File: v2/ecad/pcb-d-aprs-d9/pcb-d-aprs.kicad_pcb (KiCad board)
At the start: 4 copper layers, 100 x 80 mm, 211 parts, among them K1 Omron G6K-2F-Y 5 VDC DPDT sig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, Q1 2N7002 PA_EN -> H/L low (neve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, Q2 2N7002 relay coil, Q3 2N7002, Q4 2N7002, Q5 2N7002, Q6 2N7002, Q7 2N7002, Q8 2N7002, Q9 2N7002, U1 TLV75533PDBV 3.3 V 500 mA LDO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, U10 74LVC1G08 AND: headsets AND s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, U11 74LVC1G04 inverter (2 A 4 Y):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, U12 74LVC1G08 AND: KEY = PTT_ANY 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, U13 74LVC1G04 inverter: KEY -> SA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, U14 74LVC1G08 AND: PA_KEY = KEY A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, U15 TPS22810DRV, U16 PCA9555PW 0x26: COS, PTT stat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, U2 NiceRF SA868 VHF 2 W exciter,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, U3 CP2102N-A02-GQFN28 USB-UART b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, U4 TUSB2046BI four-port USB 2.0 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, U5 USBLC6-2SC6, U6 TI PCM2912A USB audio codec (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, U7 TI TPA6132A2 headphone amplif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, U8 TLV9062IDGK dual op amp (1 OU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, U9 74LVC1G08 AND (1 A 2 B 3 GND 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, Y1 6 MHz 3225 (CL 20 pF; C1 = C2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, Y2 6 MHz 3225 (codec clock; 18 p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

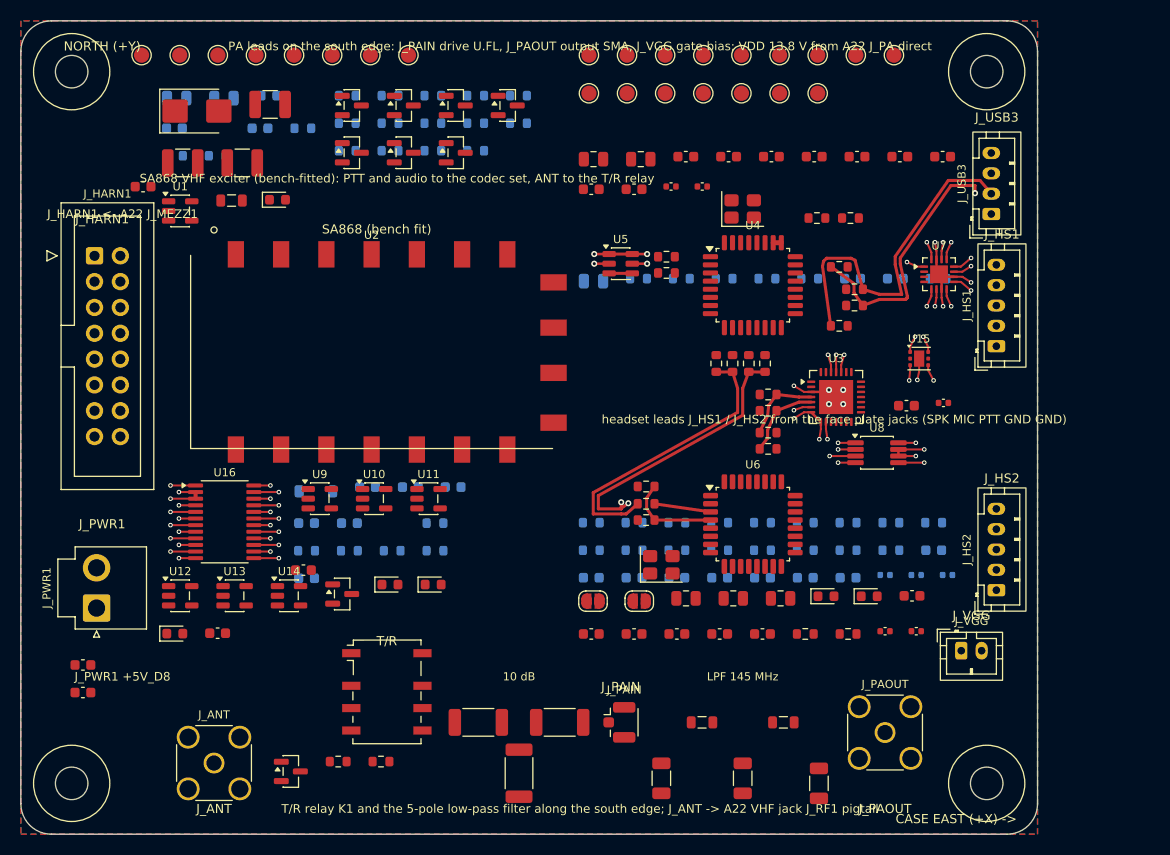
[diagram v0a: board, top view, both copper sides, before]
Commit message: feat(d): D's routed board and its regenerated schematic, tracked [MESHSAT-862]
The board is the best of the D run: 0 hard of the fifteen types, 3 unrouted
before the finish (the finish closes two of them), 5 of 5 pairs laid and
every one within 1 mm, and the schematic carries the harness pin map that
moved USB_D8 to the header's end row.

It is committed as an artefact, not as a deliverable: a routed board that
exists only in a rented box's copy directory exists nowhere, which is how
four of them were lost on 10 September. The one open and what it is are in
appendix 32.128.
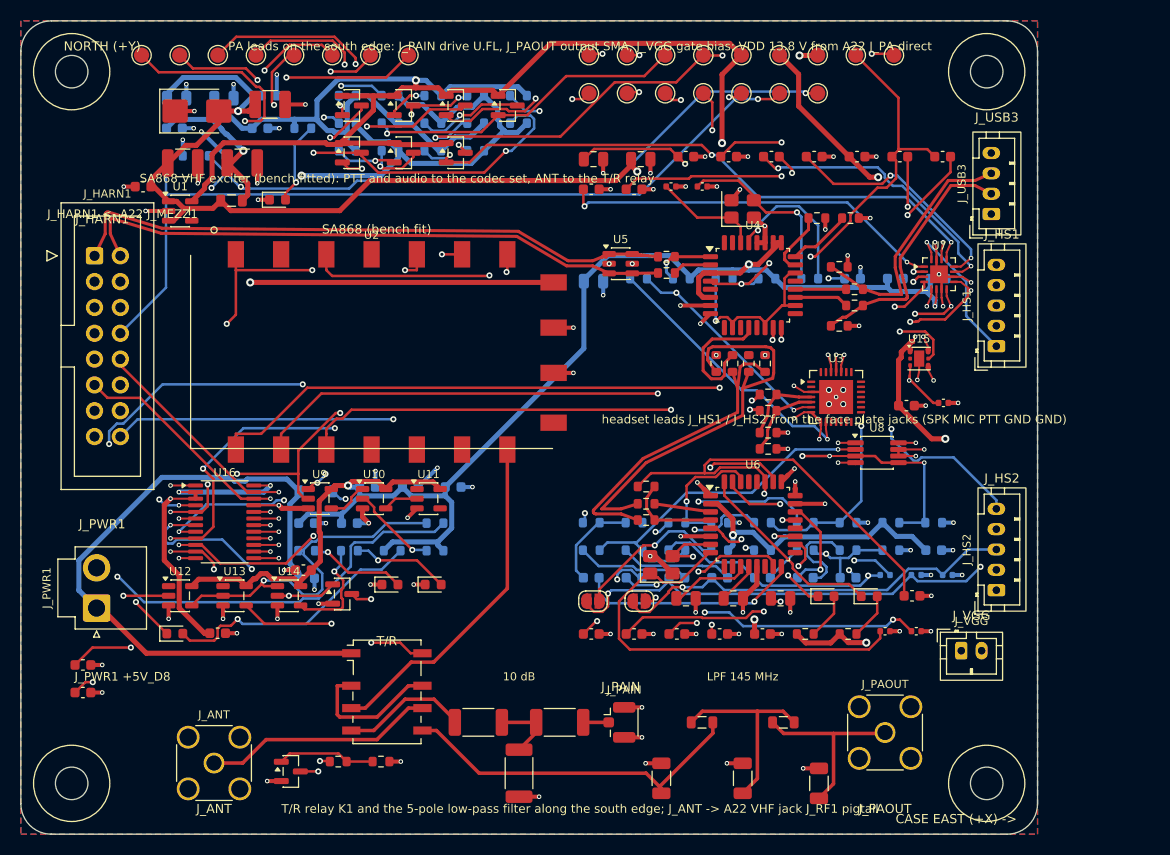
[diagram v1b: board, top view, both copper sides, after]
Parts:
- moved R12 1.60 mm to (120.0, 93.7)
- moved R13 1.60 mm to (121.6, 93.7)
- moved R20 1.60 mm to (132.0, 86.4)
- moved R21 1.60 mm to (132.0, 88.0)
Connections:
- J_HARN1 pad 1: GND -> /USB_D8_P
- J_HARN1 pad 2: GND -> /USB_D8_N
- J_HARN1 pad 3: /USB_D8_P -> GND
- J_HARN1 pad 4: /USB_D8_N -> GND
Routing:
- net /+5V_D8: track 11.4 -> 368.9 mm, vias 6 -> 11
- net /+3V3_D8: track 2.50 -> 358.9 mm, vias 1 -> 6
- net /PTT_HS2_n: track 0.00 -> 175.0 mm, vias 0 -> 6
- net /PTT_HS1_n: track 0.00 -> 164.6 mm, vias 0 -> 4
- net /PA_KEY: track 0.00 -> 160.4 mm, vias 0 -> 6
- net GND: track 20.7 -> 160.9 mm, vias 14 -> 107
- net /PA_EN: track 0.00 -> 139.3 mm, vias 0 -> 4
- net /TX_INHIBIT_n: track 0.00 -> 118.5 mm, vias 0 -> 2
- net /SA_TXD: track 1.70 -> 119.3 mm, vias 1 -> 3
- net /+3V3: track 6.39 -> 122.9 mm, vias 3 -> 4
- net /KEY: track 0.00 -> 116.3 mm, vias 0 -> 2
- net /PTT_SW_n: track 1.74 -> 115.2 mm, vias 1 -> 3
- net /ZEROIZE_HW: track 0.00 -> 110.6 mm, vias 0 -> 1
- net /AF_OUT: track 0.00 -> 97.4 mm, vias 0 -> 4
- net /SA_RXD: track 1.74 -> 86.4 mm, vias 1 -> 3
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
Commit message: feat(d): D10 is cut, 0 hard and 0 unrouted, read back on all its properties [MESHSAT-862]
meshsat-pcb-d-revA-D10: 0 hard of the fifteen types, 0 unrouted, check_pcb_d
ALL PASS on 231 checks, dc_drop MET (+5V_D8 at 1.62 percent of a 3 percent
budget), impedance 4 of 4 pairs within 10 percent of their target,
netlist_board 994 of 994, contracts ALL PASS 40 of 40, verify_deliverable ALL
PASS. The board file, the deliverable copy and the recorded sha256 all read
6a1cb1873c3973e6e506525d5891c9ae8c7691fa5028fc0c27bd4635982c795e, and the
gerber zip carries four copper layers for a four-layer board.

The last connection was closed by hand after three failed attempts to make
the router do it, each measured and recorded: a six-fold stub window on three
layers, 1.2 mm more room at the station (which costs a pair), and three times
the router passes (which gave the same three opens). The router had left
/HUB_DM1 0.28 mm short, its inner-layer track ending beside R13 pad 1 with no
via back up; the closure is a locked via there and a locked 0.25 mm track to
the pad, and the fifteen-type DRC decides, as it did for A22's VBUS20 and
C7's U3 ring.

The test copy that tool writes now goes to out/, because a project directory
that holds a second board is the B5 trap of 11 September. The suite caught
that before this commit, twice: once as an unclassified copper-laying tool
and once as a second board.

The current-phase deliverables are P3, E5, E7 and D10.

Suite 168 passed, 0 failed, 7 skipped.
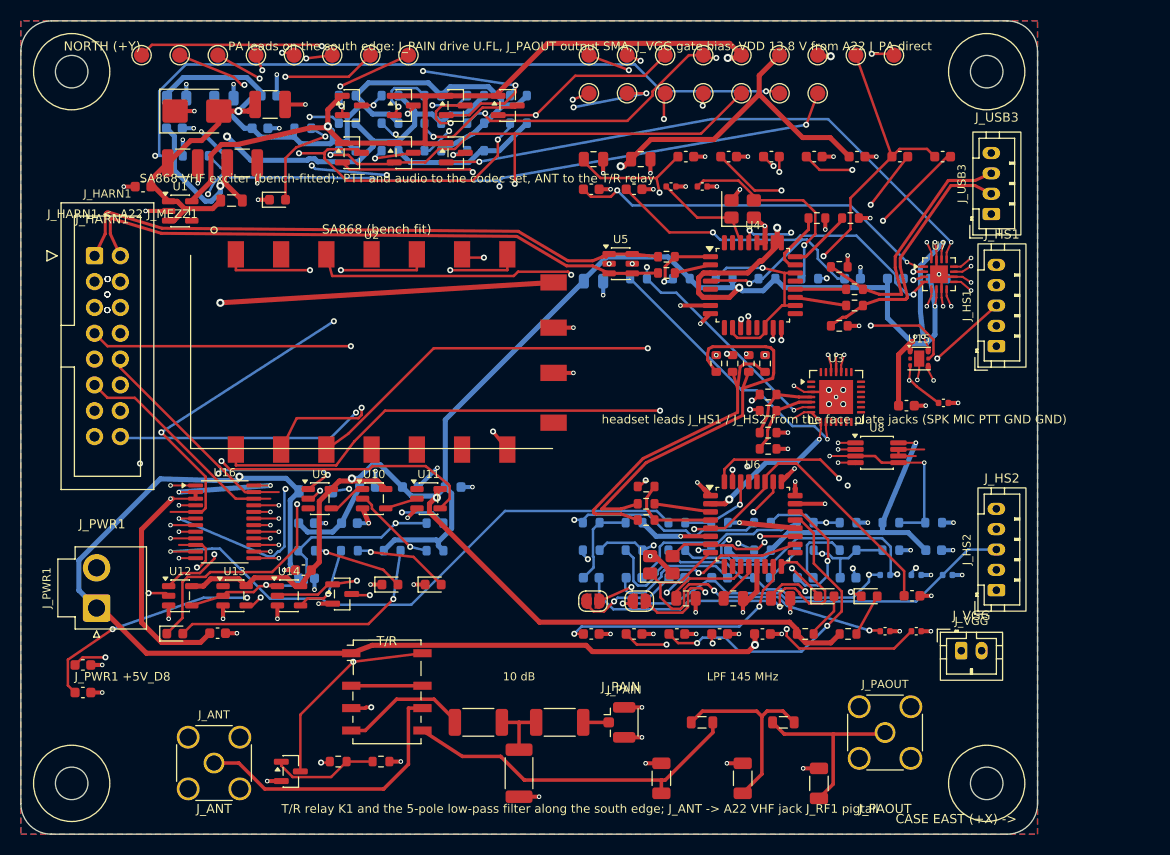
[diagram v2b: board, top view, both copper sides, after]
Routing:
- net /PTT_ANY: track 0.00 -> 41.9 mm, vias 0 -> 2
- net /SA_TXD: track 119.3 -> 94.2 mm, vias 3 -> 4
- net /PTT_HS2_n: track 175.0 -> 199.3 mm, vias 6 -> 5
- net /+3V3: track 122.9 -> 139.9 mm
- net /X_MMUTE: track 75.0 -> 58.0 mm, vias 3 -> 1
- net /HS2_BIAS_R: track 32.4 -> 15.9 mm
- net /TR_APRS: track 64.0 -> 48.7 mm, vias 1 -> 2
- net /EXP_SPARE7: track 53.6 -> 67.4 mm
- net /PCM_VDD: track 52.2 -> 38.6 mm
- net /EXP_SPARE3: track 68.7 -> 55.2 mm
- net /EXP_SPARE4: track 62.9 -> 50.4 mm
- net /PCM_VIN: track 21.8 -> 34.0 mm
- net /X_PTT_HS1_n: track 74.6 -> 63.9 mm
- net /PCM_L_AC: track 28.0 -> 18.1 mm, vias 2 -> 0
- net /MIC_SUM: track 76.3 -> 66.7 mm
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
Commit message: feat(pcb-d): D11 is cut, owner ruling 15 implemented and measured [MESHSAT-862]
0 hard, 0 unrouted, the routed-board gate ALL PASS, +5V_D8 MET, impedance 4 of 4 pairs, check_contracts 42 of
42, seventeen deliverable items, the board sha256 81614025 matching three ways.

Ruling 15 in the copper: the PWR class is back to 0.5 mm and the rail is carried at 1.7 mm (trunk) and 1.5 mm
(west branch) as locked In2 copper, sized to the current the rail's declared loads actually put in them,
1.0 A and 0.75, rather than the whole rail in one conductor. The east branch's 0.25 A is inside what the
0.5 mm class carries and needs no locked copper at all.

Ruling 9's 1.2 mm class touched 191 of the 230 pads on these nets; this touches none of them, because it is
copper and not a class width. The rail reads conductor 0.45 and pour 0.54 against their bars.
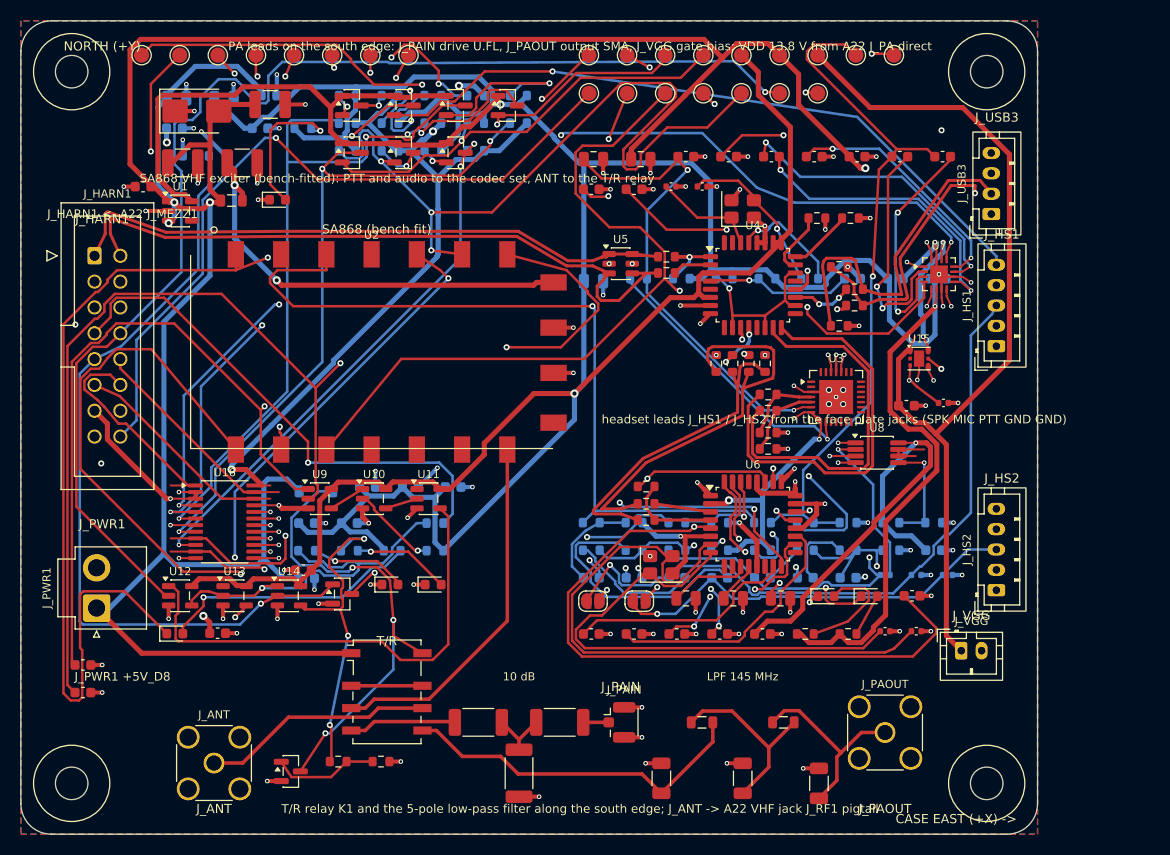
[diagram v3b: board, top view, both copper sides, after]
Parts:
- J_ANT: value antenna (SMA, pigtail to A22's VHF jack J_RF1) -> SMA jack: antenna pigtail to A22's VHF jack J_RF1
- J_HARN1: footprint IDC-Header_2x08_P2.54mm_Vertical -> IDC-Header_2x08_P2.54mm_Vertical_NarrowPad
- J_HS1: value headset 1 lead (JST-PH 1x5 to the face plate U-174/U jack): SPK GND MIC GND PTT -> JST-PH 1x5 socket: headset 1, SPK GND MIC GND PTT (the lead runs to the face plate U-174/U jack)
- J_HS2: value headset 2 lead (JST-PH 1x5 to the face plate U-174/U jack): SPK GND MIC GND PTT -> JST-PH 1x5 socket: headset 2, SPK GND MIC GND PTT (the lead runs to the face plate U-174/U jack)
- J_PAIN: value PA drive (U.FL, coax to the RA30H1317M1 input on the plate) -> U.FL socket: PA drive (coax to the RA30H1317M1 input on the plate)
- J_PAOUT: value PA output (SMA, coax from the RA30H1317M1 output on the plate) -> SMA jack: PA output (coax from the RA30H1317M1 output on the plate)
- J_PWR1: value 5 V from A22 J_MEZZ_PWR1 (JST-VH, 2 A eFuse on A22): + - -> JST-VH socket, 10 A: 5 V from A22 J_MEZZ_PWR1 (behind A22's 2 A eFuse U23): + -
- J_USB3: value spare hub port 3 (JST-PH 1x4): 5V D- D+ GND -> JST-PH 1x4 socket: spare hub port 3, 5V D- D+ GND (the lead is made up at build)
- J_VGG: value PA gate bias lead (JST-PH 1x2 to the RA30H1317M1 VGG): VGG GND -> JST-PH 1x2 socket: PA gate bias, VGG GND (the lead runs to the RA30H1317M1 VGG pin)
- moved R20 1.60 mm to (132.0, 88.0)
- moved R21 1.60 mm to (132.0, 86.4)
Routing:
- net /+3V3_D8: track 358.6 -> 425.7 mm, vias 7 -> 3
- net /PCM_VDD: track 38.6 -> 84.8 mm
- net /+5V_D8: track 360.7 -> 406.3 mm, vias 10 -> 11
- net /MIC_SUM: track 66.7 -> 107.8 mm
- net /MIC_IN: track 76.9 -> 115.1 mm
- net /PTT_HS1_n: track 161.1 -> 195.5 mm, vias 4 -> 3
- net /PA_KEY: track 163.0 -> 195.9 mm, vias 6 -> 5
- net /PA_EN: track 141.7 -> 172.7 mm, vias 4 -> 2
- net /HUB_DP2: track 8.88 -> 39.9 mm, vias 2 -> 0
- net /SA_AUDIO_ON_n: track 74.7 -> 102.7 mm, vias 3 -> 2
- net /PCM_XTO: track 33.3 -> 60.8 mm, vias 2 -> 0
- net /HUB_DM2: track 10.3 -> 37.3 mm, vias 2 -> 0
- net /+3V3: track 139.9 -> 118.6 mm, vias 4 -> 6
- net /SA_PD: track 59.7 -> 79.4 mm
- net /KEY: track 115.6 -> 135.3 mm, vias 4 -> 3
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- added copper zone on In2.Cu, net /+5V_D8
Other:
- board text added: "PCB-D APRS MEZZANINE REV A (D11)"
- board text removed: "PCB-D APRS MEZZANINE REV A (D10)"

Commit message: feat(ecad): D12 re-finished at 0 hard and 0 unrouted; its last return via is 2.25 mm and measured [MESHSAT-862]
The board comes back from the re-finish with hard 0 and unrouted 0 of the fifteen
types, every rail met, the netlist agreeing on 994 of 994, and one rule failing:
HUB_DM3's ground via sits 2.25 mm from the signal via it returns, against a
declared 1.5 mm, because all 64 sites inside that radius are on another net's
copper. The via is placed, the distance is in the log and in decision 32, and the
verdict still reads FAIL because the bar did not move to meet it.
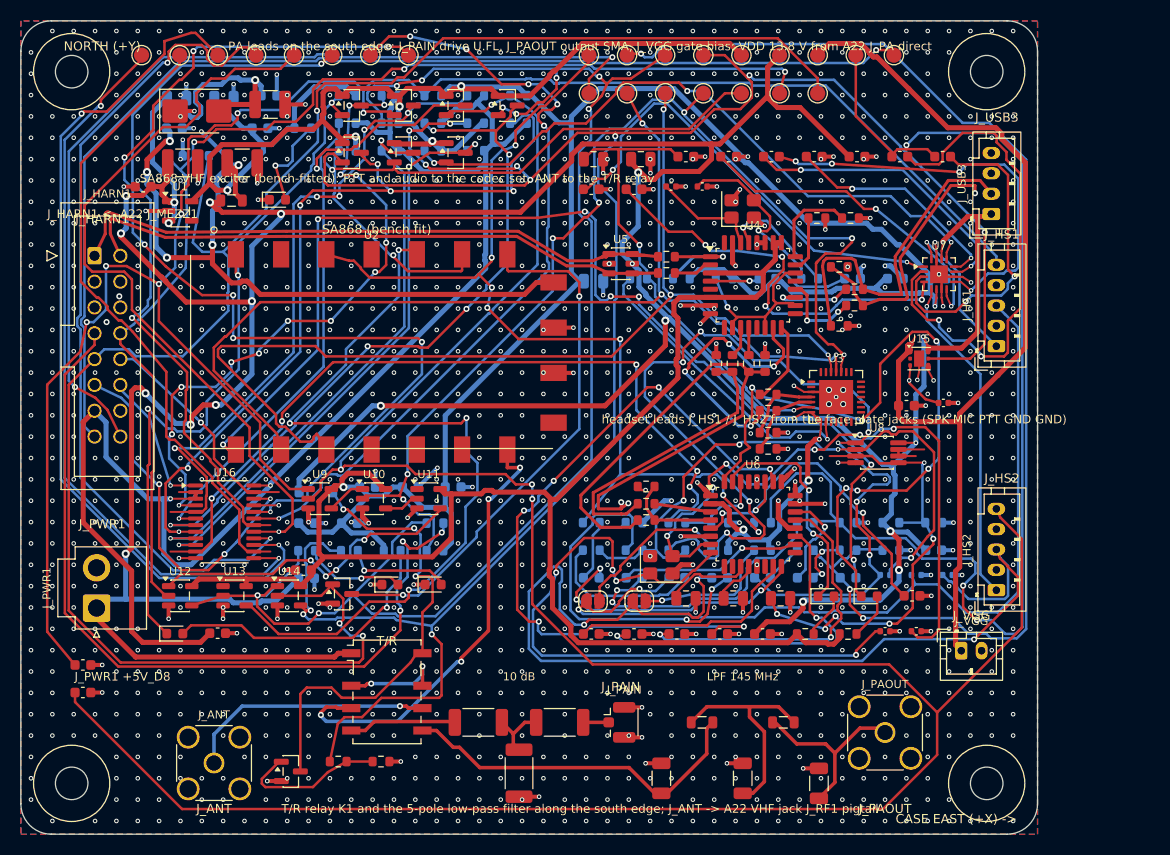
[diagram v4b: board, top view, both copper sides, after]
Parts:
- moved R12 1.60 mm to (121.6, 93.7)
- moved R13 1.60 mm to (120.0, 93.7)
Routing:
- net /HS2_MIC: track 40.9 -> 104.8 mm, vias 1 -> 3
- net /EXP_SPARE8: track 52.0 -> 104.1 mm, vias 2 -> 8
- net /MICAMP_OUT: track 48.7 -> 100.7 mm, vias 2 -> 8
- net /RX_MIX: track 69.7 -> 119.3 mm, vias 1 -> 3
- net /LED_PLAY_K: track 23.1 -> 70.0 mm, vias 2 -> 6
- net /+5V_D8: track 406.3 -> 450.8 mm, vias 11 -> 26
- net /PCM_VDD: track 84.8 -> 42.9 mm, vias 2 -> 4
- net /PTT_HS2_n: track 216.9 -> 254.6 mm, vias 2 -> 4
- net /PA_KEY: track 195.9 -> 231.1 mm, vias 5 -> 11
- net /SA_PTT_n: track 47.9 -> 81.2 mm, vias 3 -> 4
- net /EXP_SPARE4: track 50.8 -> 82.6 mm
- net /PCM_VCCP: track 40.2 -> 71.9 mm, vias 3 -> 6
- net /EXP_SPARE3: track 54.2 -> 85.8 mm
- net /HUB_DP2: track 39.9 -> 8.24 mm
- net /+3V3: track 118.6 -> 149.7 mm, vias 6 -> 2
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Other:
- board text added: "PCB-D APRS MEZZANINE REV A (D12)"
- board text removed: "PCB-D APRS MEZZANINE REV A (D11)"
